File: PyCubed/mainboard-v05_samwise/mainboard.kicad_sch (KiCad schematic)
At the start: 0 parts

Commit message: More small pycbuded changes
Fixed title block
Fixed Watchdog datasheet link (was broken)
Reduced watchdog tie in resistor value
Replaced an old ground symbol
Cleaned up some labeling
Checked some capacitor ratings
Changed fixed solar regulator input capacitor voltage rating to be higher. All capacitors should be checked and have values put in fields
Small silkscreen edits
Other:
- company: Max Holliday -> SSI
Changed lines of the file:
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@@
   (title_block
     (title "PyCubed Mainboard")
-    (date "2021-06-09")
-    (rev "v05c")
-    (company "Max Holliday")
+    (date "2024-05-04")
+    (rev "v06b")
+    (company "SSI")
   )
   (text "PyCubed" (at 212.09 177.8 0)

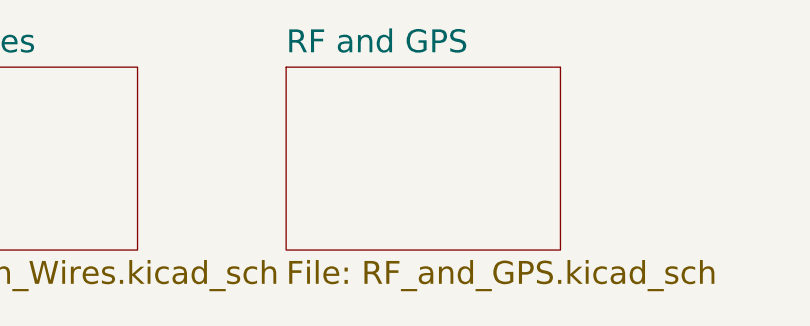
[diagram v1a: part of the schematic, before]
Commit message: Lots of changes
Some of these changes were made on schematic on previous commit, but now on the layout
Update connector pinouts:
 - Battery
 - Z solar
 - Y flex solar
 - Local RBF
Added QWIIC connector
Increased max current sense to 5A by changing R8
Changed C19, C20 to be 10uF
Changed C22 & C19 & C20's footprint and specs to all match
Added some power flags
Made sense resistor have a 4 wire kelvin connection
Silkscreen cleanup
General cleanup
All resistor k are now lowercase
Exported files:
 - pdf schematic
 - ibom
 - gerbers
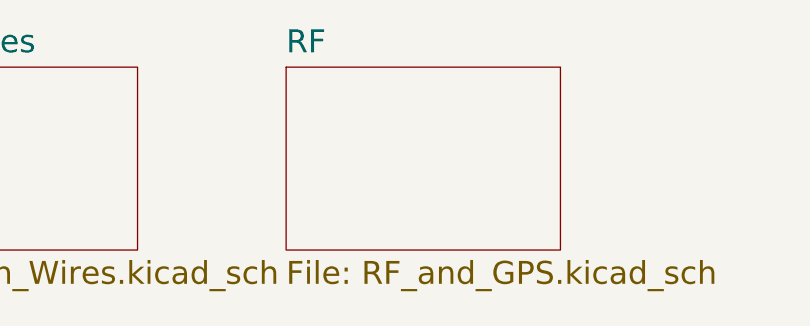
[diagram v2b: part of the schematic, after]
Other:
- sheet RF and GPS renamed RF
- company: SSI -> Stanford Student Space Initiative
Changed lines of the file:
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@@
   (title_block
     (title "PyCubed Mainboard")
-    (date "2024-05-04")
+    (date "2024-05-14")
     (rev "v06b")
-    (company "SSI")
+    (company "Stanford Student Space Initiative")
+    (comment 1 "Ethan Brinser")
   )
   (text "PyCubed" (at 212.09 177.8 0)
@@
     (stroke (width 0) (type solid))
     (fill (color 0 0 0 0.0000))
-    (property "Sheetname" "RF and GPS" (at 224.79 65.9634 0)
+    (property "Sheetname" "RF" (at 224.79 65.9634 0)
       (effects (font (size 2.54 2.54)) (justify left bottom))
     )
